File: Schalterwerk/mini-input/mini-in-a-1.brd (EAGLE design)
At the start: 80 x 30.5 mm, 21 parts, among them U2 74HC166, U5 MC7805BDTRKG, X1 DNLINK, X2 UPLINK, X3 MOLEX_530470610CON_530470610_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, X4 MOLEX_530470610CON_530470610_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

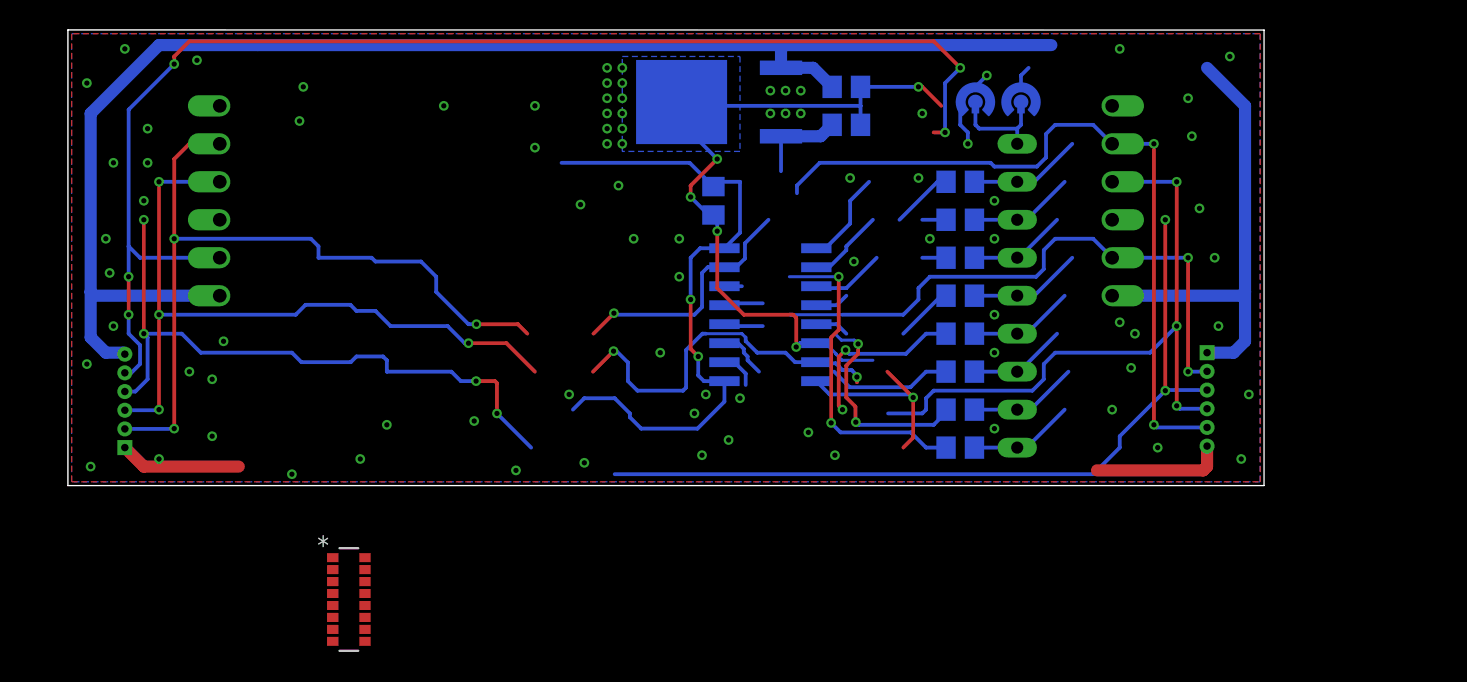
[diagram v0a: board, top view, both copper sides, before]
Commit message: Completes design for the Lampen input board.
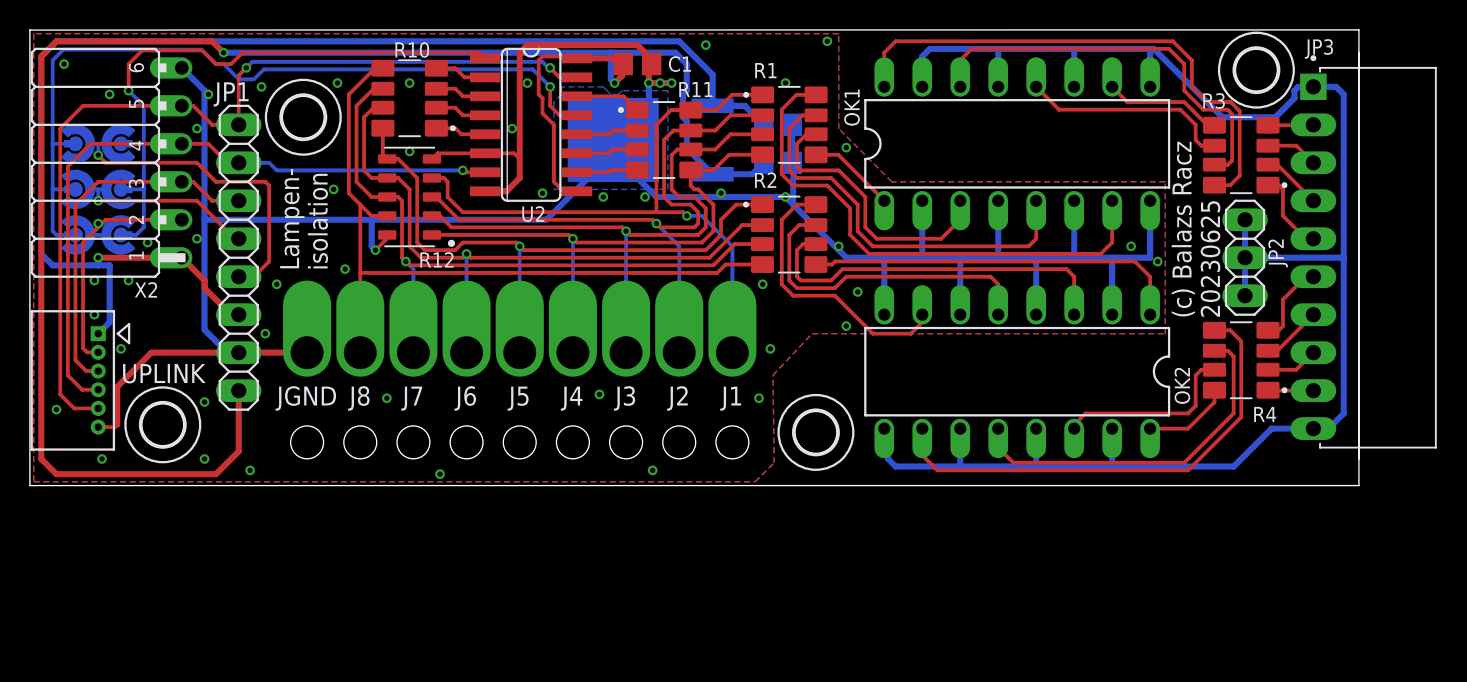
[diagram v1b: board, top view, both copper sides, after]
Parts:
- removed R5, R6, R7, R8: (no value), rcl:R0805
- removed R9: 742C163103JPRES_CTS74X_6P4X1P6_CTS-M, eagleparts:RES_CTS74X_6P4X1P6_CTS-M
- removed RN1: 10K, resistor-sil:SIL9
- removed X1: DNLINK, eagleparts:JP6F
- removed X4: MOLEX_530470610CON_530470610_MOL, eagleparts:CON_530470610_MOL
- added H1, H2, H3, H4: MOUNT-HOLE, eagleparts:MOUNT-HOLE-2,8
- added J1, J2, J3, J4, J5, J6, J7, J8, JGND: LARGE-SOLDERPADWITH-HOLE, eagleparts:LARGE-SOLDERPAD-WITH-HOLES
- added JP1: (no value), pinhead:1X08
- added JP2: (no value), pinhead:1X03
- added JP3: TE-CON-MTA150-RA-HEADER-1-640457-0, eagleparts:TE_1-640457-0
- added OK1, OK2: PC847, optocoupler:DIL16
- added R10, R11: 10k, eagleparts:RESCAXS127P508X320X70-8N
- added R12: 10k, eagleparts:RESCAV127P640X310X70-10N
- added SJ1, SJ2, SJ5, SJ6: (no value), eagleparts:SJ_RND2
- R1: value (none) -> 1k5; device rcl:R0805 -> eagleparts:RESCAXS127P508X320X70-8N
- R2: value (none) -> 10k; device rcl:R0805 -> eagleparts:RESCAXS127P508X320X70-8N
- R3, R4: value (none) -> 100; device rcl:R0805 -> eagleparts:RESCAXS127P508X320X70-8N
- SJ3, SJ4: device trainlib:SJ_RND2 -> eagleparts:SJ_RND2
- X3: value MOLEX_530470610CON_530470610_MOL -> MOLEX_530480610CON_530480610_MOL; device eagleparts:CON_530470610_MOL -> eagleparts:CON_530480610_MOL
- moved X3 74.2 mm to (2.03, 10.2), flipped to the top, turned to 270 degrees
- moved SJ3 63.3 mm to (0.51, 22.9), turned to 180 degrees
- moved X2 62.3 mm to (7.62, 24.1), flipped to the top
- moved SJ4 57.4 mm to (3.56, 19.8), turned to 0 degrees
- moved U2 20.4 mm to (31.0, 24.1), flipped to the top
- moved R3 20.0 mm to (78.5, 22.1), flipped to the top
- moved R4 19.3 mm to (78.5, 8.38), flipped to the top
- moved R1 12.0 mm to (48.3, 24.1), flipped to the top, turned to 0 degrees
- moved R2 11.5 mm to (48.2, 16.8), flipped to the top, turned to 0 degrees
- moved C1 10.5 mm to (38.1, 28.2), flipped to the top, turned to 0 degrees
- moved C6 5.23 mm to (47.5, 24.1)
- moved C5 5.23 mm to (47.5, 21.6)
- moved U5 5.23 mm to (39.0, 23.1)
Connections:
- new net DGND: JP2.1, JP2.2, JP2.3, JP3.1, JP3.10, OK1.11, OK1.13, OK1.15, OK1.9, OK2.11, OK2.13, OK2.15, OK2.9
- new net MISO-LNK: SJ5.P$2, SJ6.P$2, X2.2, X3.2
- new net N$10: OK1.5, R1.7
- new net N$11: OK1.3, R1.6
- new net N$12: OK1.1, R1.5
- new net N$15: JP3.2, R3.4
- new net N$16: JP3.3, R3.3
- new net N$17: JP3.4, R3.2
- new net N$18: JP3.5, R3.1
- new net N$19: JP3.6, R4.4
- new net N$2: J2.P$1, R1.2, R11.7, R12.3
- new net N$20: JP3.7, R4.3
- new net N$21: JP3.8, R4.2
- new net N$22: JP3.9, R4.1
- new net N$23: OK1.10, R3.5
- new net N$24: OK1.12, R3.6
- new net N$25: OK1.14, R3.7
- new net N$26: OK1.16, R3.8
- new net N$3: J3.P$1, R1.3, R11.6, R12.2
- new net N$4: J4.P$1, R1.4, R11.5, R12.1
- new net N$5: J5.P$1, R10.8, R12.6, R2.1
- new net N$6: J6.P$1, R10.7, R12.7, R2.2
- new net N$7: J7.P$1, R10.6, R12.8, R2.3
- new net N$8: J8.P$1, R10.5, R12.9, R2.4
- new net N$9: OK1.7, R1.8
- new net UD1: JP1.5, SJ2.P$2, SJ3.P$2
- new net UD2: JP1.4, SJ1.P$2, SJ4.P$2
- net +12V: now also JP1.6; no longer SJ3.P$2, X1.6, X4.6
- net +5V: now also JP1.8
- net GND: now also JGND.P$1, JP1.7, OK1.2, OK1.4, OK1.6, OK1.8, OK2.2, OK2.4, OK2.6, OK2.8, R12.10, R12.5; no longer SJ4.P$2, X1.1, X4.1
- net LATCH: now also JP1.1; no longer X1.2, X4.2
- net MISO-DN: now also SJ2.P$1, SJ4.P$1, SJ5.P$1; no longer X1.5, X4.5
- net MISO-UP: now also SJ1.P$1, SJ3.P$1, SJ6.P$1; no longer X2.2, X3.2
- net MOSI: now also JP1.3; no longer X1.4, X4.4
- net N$1: now also J1.P$1, R1.1, R11.8, R12.4; no longer RN1.1, SJ3.P$1, SJ4.P$1
- net N$27: now also OK2.10, R4.5; no longer R1.2, RN1.2
- net N$28: now also OK2.12, R4.6; no longer R2.2, RN1.3
- net N$29: now also OK2.14, R4.7; no longer R3.2, RN1.4
- net N$30: now also OK2.16, R4.8; no longer R4.2, RN1.5
- net N$31: now also OK2.7, R2.8; no longer R5.2, RN1.6
- net N$32: now also OK2.5, R2.7; no longer R6.2, RN1.7
- net N$33: now also OK2.3, R2.6; no longer R7.2, RN1.8
- net N$34: now also OK2.1, R2.5; no longer R8.2, RN1.9
- net QA: now also R10.4; no longer R1.1
- net QB: now also R10.3; no longer R2.1
- net QC: now also R10.2; no longer R3.1
- net QD: now also R10.1; no longer R4.1
- net QE: now also R11.4; no longer R5.1
- net QF: now also R11.3; no longer R6.1
- net QG: now also R11.2; no longer R7.1
- net QH: now also R11.1; no longer R8.1
- net SCK: now also JP1.2; no longer X1.3, X4.3
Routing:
- net DGND: track 0.00 -> 116.2 mm
- net GND: track 85.0 -> 182.8 mm, vias 92 -> 50
- net MOSI: track 97.5 -> 24.3 mm, vias 6 -> 0
- net SCK: track 118.1 -> 45.7 mm, vias 9 -> 1
- net +5V: track 49.8 -> 121.5 mm
- net LATCH: track 119.1 -> 60.5 mm, vias 6 -> 2
- net MISO-DN: track 95.3 -> 40.4 mm, vias 5 -> 1
- net N$8: track 0.00 -> 49.8 mm
- net N$7: track 0.00 -> 45.9 mm, vias 0 -> 1
- net N$6: track 0.00 -> 44.1 mm, vias 0 -> 1
- net +12V: track 130.9 -> 87.3 mm, vias 0 -> 1
- net N$2: track 0.00 -> 42.6 mm, vias 0 -> 1
- net N$5: track 0.00 -> 41.7 mm, vias 0 -> 1
- net N$3: track 0.00 -> 40.2 mm, vias 0 -> 1
- net N$4: track 0.00 -> 37.1 mm, vias 0 -> 1
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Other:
- board size 80 x 30.5 mm -> 88.9 x 30.5 mm
- board text added: "(c) Balazs Racz 20230625"
- board text added: "Close SJ1+SJ2+clip UD2, OR Close SJ3+SJ4+clip UD1"
- board text added: "Close SJ6 + connector=top for UPLink Close SJ5 + connector=bottom for DNLink"
- board text added: "Lampen- isolation"
- board text added: "UD1"
- board text added: "UD2"
- board text removed: "(c) Balazs Racz 20230526"
- board text removed: "I/O"
- board text removed: "UPLink NUR mit DNLink verbinden!"
